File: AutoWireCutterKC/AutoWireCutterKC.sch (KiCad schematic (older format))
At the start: 5 parts, among them J1 LCD I/O, J2 AVR-ISP-6, J2 LCD Serial

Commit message: Update uC Layout
Power is next, runout sensor planned.
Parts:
- removed J2: AVR-ISP-6, AVR-ISP-6, symbol AVR-ISP-6
- added C2: 100u, symbol CP
- added J2: ISP, symbol Conn_02x03_Odd_Even
- added J4: Conn_02x08_Top_Bottom, symbol Conn_02x08_Top_Bottom
- added J5: Stepper, symbol Conn_01x04
- C1: value C -> 100n
- renumbered J2 to J3
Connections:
- net labels added: +24V
- wire segments 49 -> 80
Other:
- moved on the sheet: C1, J1, J3, U?

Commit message: Schematic Finished
TODO: Double check connections
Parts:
- added C3, C4, C5: 1u, symbol C
- added C6: 3.3u, symbol CP1
- added J6: LCD Power, symbol Conn_01x03
- added J7: Servo, symbol Conn_01x03
- added J7: Barrel_Jack, symbol Barrel_Jack
- added U2: MCP1700_SOT23, TO_SOT_Packages_SMD:SOT-23, symbol MCP1700-5002E_SOT23
- added U3: LT1129-5.0_SOT223, TO_SOT_Packages_SMD:SOT-223-3Lead_TabPin2, symbol LT1129-5.0_SOT223
- gave numbers to parts that had none: 1
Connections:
- net labels added: +12V, +5V, +5VL
- net labels removed: +24V
- wire segments 80 -> 110
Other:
- moved on the sheet: C1, C2, J1, J2, J3, J4, J5, U1

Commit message: Working on footprints
in progress
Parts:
- removed J6: LCD Power, symbol Conn_01x03
- added J5: LCD Power, Pin_Headers:Pin_Header_Angled_1x02_Pitch2.54mm, symbol Conn_01x02
- J2: footprint (none) -> Pin_Headers:Pin_Header_Straight_2x03_Pitch2.54mm
- J3: footprint (none) -> Pin_Headers:Pin_Header_Angled_1x02_Pitch2.54mm
- J4: value Conn_02x08_Top_Bottom -> DRV8825
- J5: footprint (none) -> Pin_Headers:Pin_Header_Straight_1x04_Pitch2.54mm
- J7: footprint (none) -> Pin_Headers:Pin_Header_Angled_1x03_Pitch2.54mm
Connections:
- net +5VL: now also J5.1 (Pin_1)
- net GND: now also J5.2 (Pin_2)
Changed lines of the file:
@@
 F 0 "J3" H 4950 4050 50  0000 C CNN
 F 1 "LCD Serial" H 4950 3750 50  0000 C CNN
-F 2 "" H 4950 3950 50  0001 C CNN
+F 2 "Pin_Headers:Pin_Header_Angled_1x02_Pitch2.54mm" H 4950 3950 50  0001 C CNN
 F 3 "" H 4950 3950 50  0001 C CNN
 	1    4950 3950
@@
 F 0 "J2" H 6200 3800 50  0000 C CNN
 F 1 "ISP" H 6200 3400 50  0000 C CNN
-F 2 "" H 6150 3600 50  0001 C CNN
+F 2 "Pin_Headers:Pin_Header_Straight_2x03_Pitch2.54mm" H 6150 3600 50  0001 C CNN
 F 3 "" H 6150 3600 50  0001 C CNN
 	1    6150 3600
@@
 P 5500 4650
 F 0 "J4" H 5550 5050 50  0000 C CNN
-F 1 "Conn_02x08_Top_Bottom" H 5550 4150 50  0000 C CNN
+F 1 "DRV8825" H 5550 4150 50  0000 C CNN
 F 2 "" H 5500 4650 50  0001 C CNN
 F 3 "" H 5500 4650 50  0001 C CNN
@@
 F 0 "J5" H 6650 4850 50  0000 C CNN
 F 1 "Stepper" H 6650 4350 50  0000 C CNN
-F 2 "" H 6650 4650 50  0001 C CNN
+F 2 "Pin_Headers:Pin_Header_Straight_1x04_Pitch2.54mm" H 6650 4650 50  0001 C CNN
 F 3 "" H 6650 4650 50  0001 C CNN
 	1    6650 4650
@@
 $EndComp
 $Comp
-L Conn_01x03 J6
-U 1 1 5B1A9FB3
-P 4550 5350
-F 0 "J6" H 4550 5550 50  0000 C CNN
-F 1 "LCD Power" H 4550 5150 50  0000 C CNN
-F 2 "" H 4550 5350 50  0001 C CNN
-F 3 "" H 4550 5350 50  0001 C CNN
-	1    4550 5350
-	1    0    0    -1
-$EndComp
-$Comp
 L GND #PWR?
 U 1 1 5B1AA1E5
@@
 F 0 "J7" H 3750 6100 50  0000 C CNN
 F 1 "Servo" H 3750 5700 50  0000 C CNN
-F 2 "" H 3750 5900 50  0001 C CNN
+F 2 "Pin_Headers:Pin_Header_Angled_1x03_Pitch2.54mm" H 3750 5900 50  0001 C CNN
 F 3 "" H 3750 5900 50  0001 C CNN
 	1    3750 5900
@@
 	6950 5050 5800 5050
 Wire Wire Line
-	3450 4850 3900 4850
-Wire Wire Line
-	3900 4850 3900 5350
-Wire Wire Line
-	3900 5350 4350 5350
-Wire Wire Line
 	3850 5450 4350 5450
 Wire Wire Line
 	4150 5450 4150 5500
 Wire Wire Line
-	4250 5050 4250 5250
-Wire Wire Line
-	4250 5250 4350 5250
+	4250 5150 4250 5350
+Wire Wire Line
+	4250 5350 4350 5350
 Wire Wire Line
 	3450 4950 3750 4950
@@
 L +5VL #PWR?
 U 1 1 5B1EDDCC
-P 4250 5050
-F 0 "#PWR?" H 4250 4900 50  0001 C CNN
-F 1 "+5VL" H 4250 5190 50  0000 C CNN
-F 2 "" H 4250 5050 50  0001 C CNN
-F 3 "" H 4250 5050 50  0001 C CNN
-	1    4250 5050
+P 4250 5150
+F 0 "#PWR?" H 4250 5000 50  0001 C CNN
+F 1 "+5VL" H 4250 5290 50  0000 C CNN
+F 2 "" H 4250 5150 50  0001 C CNN
+F 3 "" H 4250 5150 50  0001 C CNN
+	1    4250 5150
 	1    0    0    -1
 $EndComp
@@
 	1    0    0    -1
 $EndComp
+$Comp
+L Conn_01x02 J5
+U 1 1 5B1EE683
+P 4550 5350
+F 0 "J5" H 4550 5450 50  0000 C CNN
+F 1 "LCD Power" H 4550 5150 50  0000 C CNN
+F 2 "Pin_Headers:Pin_Header_Angled_1x02_Pitch2.54mm" H 4550 5350 50  0001 C CNN
+F 3 "" H 4550 5350 50  0001 C CNN
+	1    4550 5350
+	1    0    0    -1
+$EndComp

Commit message: Finished Footprints
Refer to sch for generating BOM
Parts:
- removed J4: DRV8825, symbol Conn_02x08_Top_Bottom
- added A1: Pololu_Breakout_DRV8825, Module:Pololu_Breakout-16_15.2x20.3mm, symbol Pololu_Breakout_DRV8825
- J1: footprint (none) -> Pin_Headers:Pin_Header_Straight_2x04_Pitch2.54mm
- J8: renamed from J7; footprint (none) -> Connectors:Barrel_Jack_CUI_PJ-102AH
- U3: footprint TO_SOT_Packages_SMD:SOT-223-3Lead_TabPin2 -> TO_SOT_Packages_SMD:SOT-223
- renumbered J7 to J6, J5 to J9
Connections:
- net +12V: now also C2.1, A1.8 (VMOT)
- net +5VL: now also A1.10 (M0), A1.11 (M1), A1.12 (M2), A1.13 (~RST), A1.14 (~SLP)
- net GND: now also A1.1 (GND), A1.7 (GND)
- net at U1.1 ((PCINT19/OC2B/INT1)PD3): now also A1.16 (DIR)
- net at U1.2 ((PCINT20/XCK/T0)PD4): now also A1.15 (STEP)
- net at U1.32 ((PCINT18/INT0)PD2): now also A1.9 (~EN)
- net at J9.1 (Pin_1): now also A1.4 (A1)
- net at J9.2 (Pin_2): now also A1.3 (A2)
- net at J9.3 (Pin_3): now also A1.5 (B1)
- net at J9.4 (Pin_4): now also A1.6 (B2)
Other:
- moved on the sheet: C2, J9

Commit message: PCB Populated
Traces needed
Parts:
- C1, C3, C4, C5: footprint (none) -> Capacitors_SMD:C_0805_HandSoldering
- C2: footprint (none) -> Capacitors_SMD:CP_Elec_6.3x7.7
- C6: footprint (none) -> Capacitors_Tantalum_SMD:CP_Tantalum_Case-B_EIA-3528-21_Hand
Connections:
- net +5V: now also J6.2 (Pin_2); no longer J6.3 (Pin_3)
- net GND: now also J6.3 (Pin_3); no longer J6.1 (Pin_1)
- net at U1.10 ((PCINT22/OC0A/AIN0)PD6): now also J6.1 (Pin_1); no longer J6.2 (Pin_2)
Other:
- moved on the sheet: J6
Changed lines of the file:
@@
 LIBS:valves
 LIBS:Driver_Motor
+LIBS:pololu-drv8825
 LIBS:AutoWireCutterKC-cache
 EELAYER 25 0
@@
 F 0 "C1" H 1425 4650 50  0000 L CNN
 F 1 "100n" H 1425 4450 50  0000 L CNN
-F 2 "" H 1438 4400 50  0001 C CNN
+F 2 "Capacitors_SMD:C_0805_HandSoldering" H 1438 4400 50  0001 C CNN
 F 3 "" H 1400 4550 50  0001 C CNN
 	1    1400 4550
@@
 F 0 "C2" H 6175 4300 50  0000 L CNN
 F 1 "100u" H 6175 4100 50  0000 L CNN
-F 2 "" H 6188 4050 50  0001 C CNN
+F 2 "Capacitors_SMD:CP_Elec_6.3x7.7" H 6188 4050 50  0001 C CNN
 F 3 "" H 6150 4200 50  0001 C CNN
 	1    6150 4200
@@
 L Conn_01x03 J6
 U 1 1 5B1AA4B7
-P 3750 5900
-F 0 "J6" H 3750 6100 50  0000 C CNN
-F 1 "Servo" H 3750 5700 50  0000 C CNN
-F 2 "Pin_Headers:Pin_Header_Angled_1x03_Pitch2.54mm" H 3750 5900 50  0001 C CNN
-F 3 "" H 3750 5900 50  0001 C CNN
-	1    3750 5900
-	0    1    1    0
+P 4100 6000
+F 0 "J6" H 4100 6200 50  0000 C CNN
+F 1 "Servo" H 4100 5800 50  0000 C CNN
+F 2 "Pin_Headers:Pin_Header_Angled_1x03_Pitch2.54mm" H 4100 6000 50  0001 C CNN
+F 3 "" H 4100 6000 50  0001 C CNN
+	1    4100 6000
+	1    0    0    -1
 $EndComp
 $Comp
@@
 F 0 "C3" H 8475 4750 50  0000 L CNN
 F 1 "1u" H 8475 4550 50  0000 L CNN
-F 2 "" H 8488 4500 50  0001 C CNN
+F 2 "Capacitors_SMD:C_0805_HandSoldering" H 8488 4500 50  0001 C CNN
 F 3 "" H 8450 4650 50  0001 C CNN
 	1    8450 4650
@@
 F 0 "C5" H 8525 3950 50  0000 L CNN
 F 1 "1u" H 8525 3750 50  0000 L CNN
-F 2 "" H 8538 3700 50  0001 C CNN
+F 2 "Capacitors_SMD:C_0805_HandSoldering" H 8538 3700 50  0001 C CNN
 F 3 "" H 8500 3850 50  0001 C CNN
 	1    8500 3850
@@
 F 0 "C4" H 9325 4750 50  0000 L CNN
 F 1 "1u" H 9325 4550 50  0000 L CNN
-F 2 "" H 9338 4500 50  0001 C CNN
+F 2 "Capacitors_SMD:C_0805_HandSoldering" H 9338 4500 50  0001 C CNN
 F 3 "" H 9300 4650 50  0001 C CNN
 	1    9300 4650
@@
 F 0 "C6" H 9425 3950 50  0000 L CNN
 F 1 "3.3u" H 9425 3750 50  0000 L CNN
-F 2 "" H 9400 3850 50  0001 C CNN
+F 2 "Capacitors_Tantalum_SMD:CP_Tantalum_Case-B_EIA-3528-21_Hand" H 9400 3850 50  0001 C CNN
 F 3 "" H 9400 3850 50  0001 C CNN
 	1    9400 3850
@@
 	3450 4950 3750 4950
 Wire Wire Line
-	3750 4950 3750 5700
-Wire Wire Line
-	3850 5700 3850 5450
+	3750 4950 3750 5900
+Wire Wire Line
+	3850 5450 3850 6100
 Connection ~ 4150 5450
 Wire Wire Line
-	3650 5700 3650 5400
+	3650 5400 3650 6000
 Wire Wire Line
 	3650 5400 3300 5400
@@
 Wire Wire Line
 	5300 4150 5300 4800
+Wire Wire Line
+	3750 5900 3900 5900
+Wire Wire Line
+	3650 6000 3900 6000
+Wire Wire Line
+	3850 6100 3900 6100
 $EndSCHEMATC

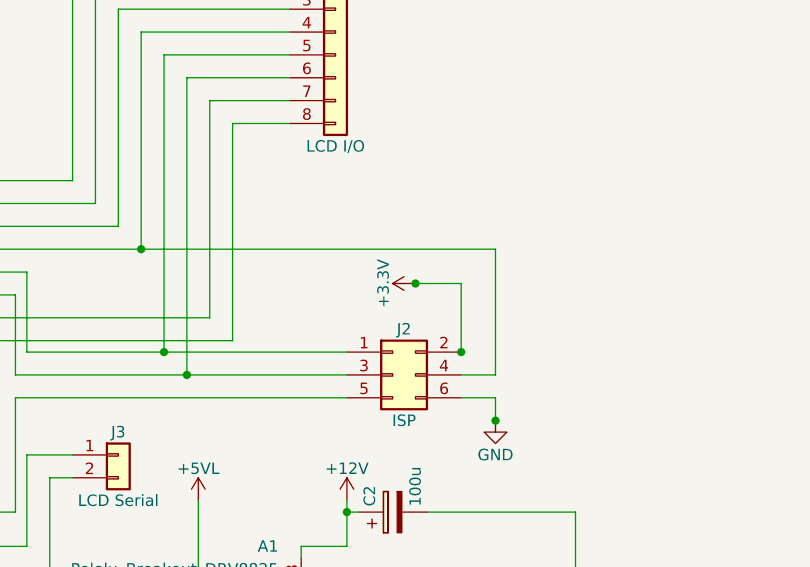
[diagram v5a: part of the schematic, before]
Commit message: PCB Redesign
Started on traces
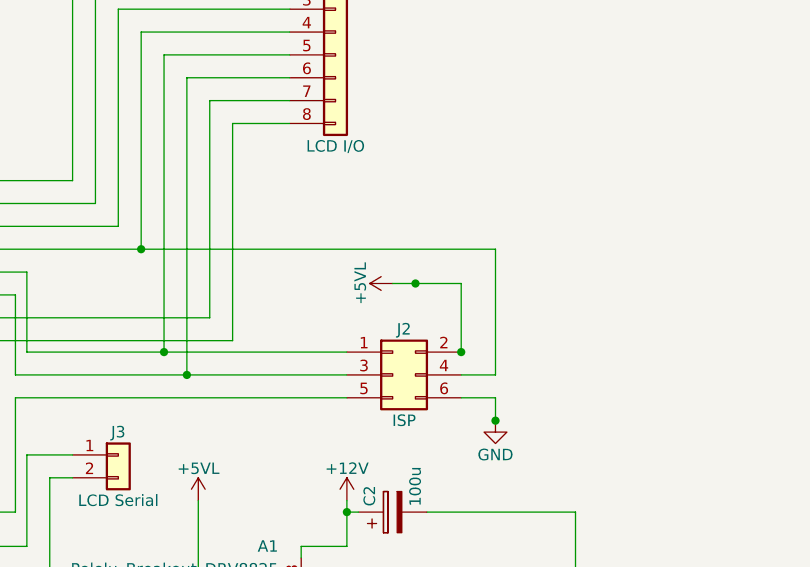
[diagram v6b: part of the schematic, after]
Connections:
- net +3V3 is gone; now on net +5VL: J2.2 (Pin_2)
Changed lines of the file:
@@
-$EndComp
-$Comp
-L +3.3V #PWR01
-U 1 1 5B16A8A1
-P 6250 3200
-F 0 "#PWR01" H 6250 3050 50  0001 C CNN
-F 1 "+3.3V" H 6250 3340 50  0000 C CNN
-F 2 "" H 6250 3200 50  0001 C CNN
-F 3 "" H 6250 3200 50  0001 C CNN
-	1    6250 3200
-	0    -1   -1   0
 $EndComp
 $Comp
@@
 	6450 3200 6450 3500
 Wire Wire Line
-	6250 3200 6450 3200
+	6150 3200 6450 3200
 Wire Wire Line
 	1550 2850 1450 2850
@@
 Wire Wire Line
 	3850 6100 3900 6100
+$Comp
+L +5VL #PWR?
+U 1 1 5B212B86
+P 6150 3200
+F 0 "#PWR?" H 6150 3050 50  0001 C CNN
+F 1 "+5VL" H 6150 3340 50  0000 C CNN
+F 2 "" H 6150 3200 50  0001 C CNN
+F 3 "" H 6150 3200 50  0001 C CNN
+	1    6150 3200
+	0    -1   -1   0
+$EndComp
 $EndSCHEMATC

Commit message: Rewiring - Layout changed again...
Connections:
- net at J9.1 (Pin_1): now also A1.3 (A2); no longer A1.4 (A1)
- net at J9.2 (Pin_2): now also A1.4 (A1); no longer A1.3 (A2)
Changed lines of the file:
@@
 $EndComp
 $Comp
-L GND #PWR02
+L GND #PWR01
 U 1 1 5B16A938
 P 1250 5050
-F 0 "#PWR02" H 1250 4800 50  0001 C CNN
+F 0 "#PWR01" H 1250 4800 50  0001 C CNN
 F 1 "GND" H 1250 4900 50  0000 C CNN
 F 2 "" H 1250 5050 50  0001 C CNN
@@
 $EndComp
 $Comp
-L GND #PWR03
+L GND #PWR02
 U 1 1 5B16B18B
 P 6600 3800
-F 0 "#PWR03" H 6600 3550 50  0001 C CNN
+F 0 "#PWR02" H 6600 3550 50  0001 C CNN
 F 1 "GND" H 6600 3650 50  0000 C CNN
 F 2 "" H 6600 3800 50  0001 C CNN
@@
 $EndComp
 $Comp
-L GND #PWR04
+L GND #PWR03
 U 1 1 5B18046F
 P 6950 5050
-F 0 "#PWR04" H 6950 4800 50  0001 C CNN
+F 0 "#PWR03" H 6950 4800 50  0001 C CNN
 F 1 "GND" H 6950 4900 50  0000 C CNN
 F 2 "" H 6950 5050 50  0001 C CNN
@@
 $EndComp
 $Comp
-L GND #PWR05
+L GND #PWR04
 U 1 1 5B1AA1E5
 P 4150 5500
-F 0 "#PWR05" H 4150 5250 50  0001 C CNN
+F 0 "#PWR04" H 4150 5250 50  0001 C CNN
 F 1 "GND" H 4150 5350 50  0000 C CNN
 F 2 "" H 4150 5500 50  0001 C CNN
@@
 $EndComp
 $Comp
-L +5V #PWR06
+L +5V #PWR05
 U 1 1 5B1AA79B
 P 3300 5500
-F 0 "#PWR06" H 3300 5350 50  0001 C CNN
+F 0 "#PWR05" H 3300 5350 50  0001 C CNN
 F 1 "+5V" H 3300 5640 50  0000 C CNN
 F 2 "" H 3300 5500 50  0001 C CNN
@@
 $EndComp
 $Comp
-L +12V #PWR07
+L +12V #PWR06
 U 1 1 5B1EB3CF
 P 9350 2800
-F 0 "#PWR07" H 9350 2650 50  0001 C CNN
+F 0 "#PWR06" H 9350 2650 50  0001 C CNN
 F 1 "+12V" H 9350 2940 50  0000 C CNN
 F 2 "" H 9350 2800 50  0001 C CNN
@@
 $EndComp
 $Comp
-L GND #PWR08
+L GND #PWR07
 U 1 1 5B1EB405
 P 9000 2800
-F 0 "#PWR08" H 9000 2550 50  0001 C CNN
+F 0 "#PWR07" H 9000 2550 50  0001 C CNN
 F 1 "GND" H 9000 2650 50  0000 C CNN
 F 2 "" H 9000 2800 50  0001 C CNN
@@
 $EndComp
 $Comp
-L GND #PWR09
+L GND #PWR08
 U 1 1 5B1EC3EE
 P 8950 4050
-F 0 "#PWR09" H 8950 3800 50  0001 C CNN
+F 0 "#PWR08" H 8950 3800 50  0001 C CNN
 F 1 "GND" H 8950 3900 50  0000 C CNN
 F 2 "" H 8950 4050 50  0001 C CNN
@@
 $EndComp
 $Comp
-L GND #PWR010
+L GND #PWR09
 U 1 1 5B1EC424
 P 8950 4850
-F 0 "#PWR010" H 8950 4600 50  0001 C CNN
+F 0 "#PWR09" H 8950 4600 50  0001 C CNN
 F 1 "GND" H 8950 4700 50  0000 C CNN
 F 2 "" H 8950 4850 50  0001 C CNN
@@
 $EndComp
 $Comp
-L +5V #PWR011
+L +5V #PWR010
 U 1 1 5B1EC45A
 P 9700 3650
-F 0 "#PWR011" H 9700 3500 50  0001 C CNN
+F 0 "#PWR010" H 9700 3500 50  0001 C CNN
 F 1 "+5V" H 9700 3790 50  0000 C CNN
 F 2 "" H 9700 3650 50  0001 C CNN
@@
 $EndComp
 $Comp
-L +12V #PWR012
+L +12V #PWR011
 U 1 1 5B1EC490
 P 8150 4450
-F 0 "#PWR012" H 8150 4300 50  0001 C CNN
+F 0 "#PWR011" H 8150 4300 50  0001 C CNN
 F 1 "+12V" H 8150 4590 50  0000 C CNN
 F 2 "" H 8150 4450 50  0001 C CNN
@@
 $EndComp
 $Comp
-L +12V #PWR013
+L +12V #PWR012
 U 1 1 5B1EC4C6
 P 8300 3650
-F 0 "#PWR013" H 8300 3500 50  0001 C CNN
+F 0 "#PWR012" H 8300 3500 50  0001 C CNN
 F 1 "+12V" H 8300 3790 50  0000 C CNN
 F 2 "" H 8300 3650 50  0001 C CNN
@@
 $EndComp
 $Comp
-L +5VL #PWR014
+L +5VL #PWR013
 U 1 1 5B1EDDCC
 P 4250 5150
-F 0 "#PWR014" H 4250 5000 50  0001 C CNN
+F 0 "#PWR013" H 4250 5000 50  0001 C CNN
 F 1 "+5VL" H 4250 5290 50  0000 C CNN
 F 2 "" H 4250 5150 50  0001 C CNN
@@
 $EndComp
 $Comp
-L +5VL #PWR015
+L +5VL #PWR014
 U 1 1 5B1EDE02
 P 1350 2750
-F 0 "#PWR015" H 1350 2600 50  0001 C CNN
+F 0 "#PWR014" H 1350 2600 50  0001 C CNN
 F 1 "+5VL" H 1350 2890 50  0000 C CNN
 F 2 "" H 1350 2750 50  0001 C CNN
@@
 $EndComp
 $Comp
-L +5VL #PWR016
+L +5VL #PWR015
 U 1 1 5B1EDFD3
 P 9600 4450
-F 0 "#PWR016" H 9600 4300 50  0001 C CNN
+F 0 "#PWR015" H 9600 4300 50  0001 C CNN
 F 1 "+5VL" H 9600 4590 50  0000 C CNN
 F 2 "" H 9600 4450 50  0001 C CNN
@@
 $EndComp
 $Comp
-L +12V #PWR017
+L +12V #PWR016
 U 1 1 5B1EE30F
 P 5950 4150
-F 0 "#PWR017" H 5950 4000 50  0001 C CNN
+F 0 "#PWR016" H 5950 4000 50  0001 C CNN
 F 1 "+12V" H 5950 4290 50  0000 C CNN
 F 2 "" H 5950 4150 50  0001 C CNN
@@
 $EndComp
 $Comp
-L GND #PWR018
+L GND #PWR017
 U 1 1 5B1F9E36
 P 5800 5900
-F 0 "#PWR018" H 5800 5650 50  0001 C CNN
+F 0 "#PWR017" H 5800 5650 50  0001 C CNN
 F 1 "GND" H 5800 5750 50  0000 C CNN
 F 2 "" H 5800 5900 50  0001 C CNN
@@
 Connection ~ 6450 3500
 Wire Wire Line
-	6150 4900 6350 4900
-Wire Wire Line
-	6350 4900 6350 4950
-Wire Wire Line
-	6350 4950 6400 4950
-Wire Wire Line
-	6150 5000 6350 5000
-Wire Wire Line
-	6350 5000 6350 5050
-Wire Wire Line
-	6350 5050 6400 5050
-Wire Wire Line
 	6150 5200 6350 5200
 Wire Wire Line
@@
 	5750 4350 5750 4400
 $Comp
-L +5VL #PWR019
+L +5VL #PWR018
 U 1 1 5B1FAD0F
 P 5100 5450
-F 0 "#PWR019" H 5100 5300 50  0001 C CNN
+F 0 "#PWR018" H 5100 5300 50  0001 C CNN
 F 1 "+5VL" H 5100 5590 50  0000 C CNN
 F 2 "" H 5100 5450 50  0001 C CNN
@@
 	9250 3650 9700 3650
 $Comp
-L +5VL #PWR020
+L +5VL #PWR019
 U 1 1 5B1FD55B
 P 5300 4150
-F 0 "#PWR020" H 5300 4000 50  0001 C CNN
+F 0 "#PWR019" H 5300 4000 50  0001 C CNN
 F 1 "+5VL" H 5300 4290 50  0000 C CNN
 F 2 "" H 5300 4150 50  0001 C CNN
@@
 	3850 6100 3900 6100
 $Comp
-L +5VL #PWR?
+L +5VL #PWR020
 U 1 1 5B212B86
 P 6150 3200
-F 0 "#PWR?" H 6150 3050 50  0001 C CNN
+F 0 "#PWR020" H 6150 3050 50  0001 C CNN
 F 1 "+5VL" H 6150 3340 50  0000 C CNN
 F 2 "" H 6150 3200 50  0001 C CNN
@@
 	0    -1   -1   0
 $EndComp
+Wire Wire Line
+	6150 5000 6250 5000
+Wire Wire Line
+	6250 5000 6250 4950
+Wire Wire Line
+	6250 4950 6400 4950
+Wire Wire Line
+	6150 4900 6350 4900
+Wire Wire Line
+	6350 4900 6350 5050
+Wire Wire Line
+	6350 5050 6400 5050
 $EndSCHEMATC

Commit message: Schematic almost done
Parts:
- added M1, M2, M3: Conn_01x01_Male, symbol Conn_01x01_Male
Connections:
- net GND: now also M1.1 (Pin_1), M2.1 (Pin_1), M3.1 (Pin_1)
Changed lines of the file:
@@
 Wire Wire Line
 	6350 5050 6400 5050
+$Comp
+L Conn_01x01_Male M1
+U 1 1 5B21AE9D
+P 13200 2350
+F 0 "M1" H 13200 2450 50  0000 C CNN
+F 1 "Conn_01x01_Male" H 13200 2250 50  0000 C CNN
+F 2 "" H 13200 2350 50  0001 C CNN
+F 3 "" H 13200 2350 50  0001 C CNN
+	1    13200 2350
+	1    0    0    -1
+$EndComp
+$Comp
+L Conn_01x01_Male M2
+U 1 1 5B21AFA3
+P 13200 2700
+F 0 "M2" H 13200 2800 50  0000 C CNN
+F 1 "Conn_01x01_Male" H 13200 2600 50  0000 C CNN
+F 2 "" H 13200 2700 50  0001 C CNN
+F 3 "" H 13200 2700 50  0001 C CNN
+	1    13200 2700
+	1    0    0    -1
+$EndComp
+$Comp
+L Conn_01x01_Male M3
+U 1 1 5B21B010
+P 13200 2950
+F 0 "M3" H 13200 3050 50  0000 C CNN
+F 1 "Conn_01x01_Male" H 13200 2850 50  0000 C CNN
+F 2 "" H 13200 2950 50  0001 C CNN
+F 3 "" H 13200 2950 50  0001 C CNN
+	1    13200 2950
+	1    0    0    -1
+$EndComp
+$Comp
+L GND #PWR?
+U 1 1 5B21B02C
+P 13700 2700
+F 0 "#PWR?" H 13700 2450 50  0001 C CNN
+F 1 "GND" H 13700 2550 50  0000 C CNN
+F 2 "" H 13700 2700 50  0001 C CNN
+F 3 "" H 13700 2700 50  0001 C CNN
+	1    13700 2700
+	0    -1   -1   0
+$EndComp
+Wire Wire Line
+	13400 2700 13700 2700
+Wire Wire Line
+	13550 2350 13550 2950
+Wire Wire Line
+	13550 2350 13400 2350
+Wire Wire Line
+	13550 2950 13400 2950
+Connection ~ 13550 2700
 $EndSCHEMATC
